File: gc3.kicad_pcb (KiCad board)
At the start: 4 copper layers, 104.6 x 77.2 mm, 204 parts, among them J1 JACK_2P, J2 DM3AT-SF-PEJM5, P1 TESTPOINT, P10 UART1, P11 CONN_01X01, P12 CONN_01X01, P13 CONN_01X01, P14 CONN_01X01, P15 TESTPOINT, P16 TESTPOINT, P17 GPIO, P18 USB_A, P19 USB_OTG, P2 TESTPOINT, P3 TESTPOINT, P4 TESTPOINT, P5 TESTPOINT, P6 TESTPOINT, P7 LCD, P8 JTAG, P9 UART0, SW1 PWR_ON, SW2 RESET, SW3 VOL+, SW4 VOL-, SW5 MENU, SW6 ENTER, SW7 HOME, U1 TPS62290, U2 axp209, U3 TPS62290, U4 a13, U5 h5tq2g63bfr, U6 TPS2552, U8 TPS2552, Y1 24MHz/20pF/10ppm

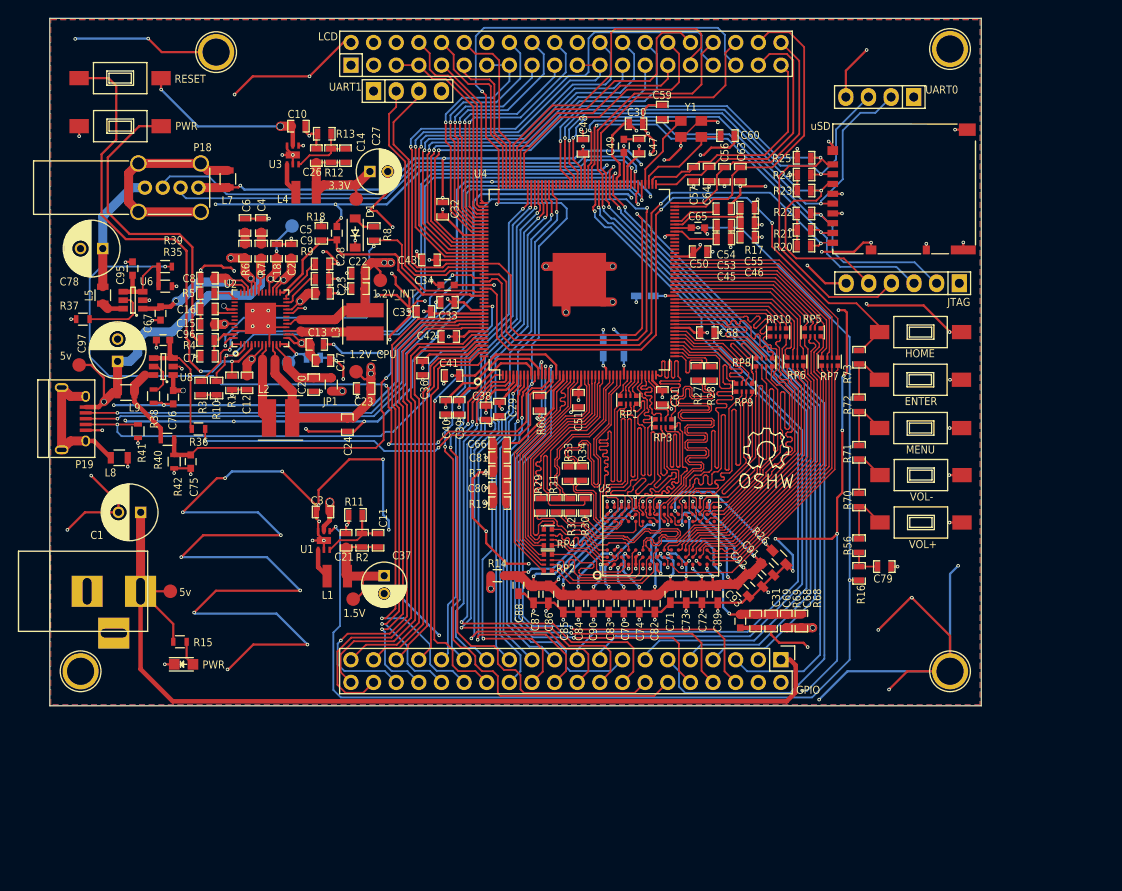
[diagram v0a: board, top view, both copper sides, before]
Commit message: clean sch and add resistor array
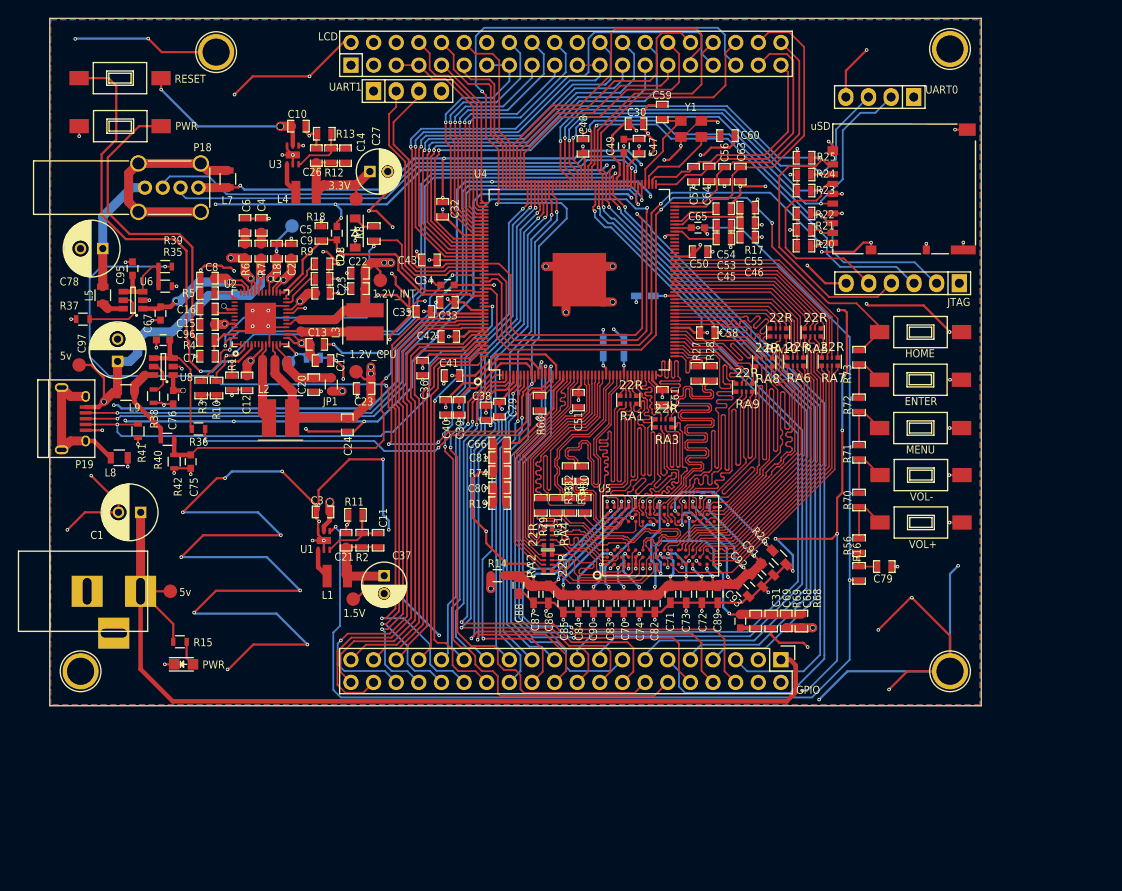
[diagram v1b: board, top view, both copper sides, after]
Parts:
- removed ?: Symbol_OSHW-Logo_SilkScreen, Symbols:Symbol_OSHW-Logo_SilkScreen
- removed RP1, RP10, RP2, RP3, RP4, RP5, RP6, RP7, RP8, RP9: R_PACK4, EXB28V:EXB28V
- added RA1: 22R, EXB28V:EXB28V, F.Cu at (170.5, 100.4)
- added RA10: 22R, EXB28V:EXB28V, F.Cu at (187.3, 92.8)
- added RA2: 22R, EXB28V:EXB28V, F.Cu at (162.9, 118.2)
- added RA3: 22R, EXB28V:EXB28V, F.Cu at (174.5, 103.0)
- added RA4: 22R, EXB28V:EXB28V, F.Cu at (162.0, 117.2)
- added RA5: 22R, EXB28V:EXB28V, F.Cu at (191.2, 92.8)
- added RA6: 22R, EXB28V:EXB28V, F.Cu at (189.3, 96.1)
- added RA7: 22R, EXB28V:EXB28V, F.Cu at (193.1, 96.1)
- added RA8: 22R, EXB28V:EXB28V, F.Cu at (185.8, 96.2)
- added RA9: 22R, EXB28V:EXB28V, F.Cu at (183.5, 99.0)
- C20: value NA or 10uF/6.3V -> 10uF/6.3V
- C27, C37: value 100uF/25V -> 100uF
- C47: value 0.1uF/6.3V -> 0.1uF
- C53: value 10uF/6.3V -> 0.1uF/6.3V
- C54: value 1uF/6.3V -> 0.1uF/6.3V
- C56, C57, C63, C64, C79: value 1nF -> 1uF
- D2: value PWR -> LED
- J1: value JACK_2P -> JACK
- L2, L3: value 2.2uH/1.5A -> 2.2uH
- P11, P12, P13, P14: value CONN_01X01 -> GND
- P16: value TESTPOINT -> TEESTPOINT
- R12: value 100K -> 100k
- R13: value 22K -> 22k
- Y1: value 24MHz/20pF/10ppm -> 24MHz/20pF/20ppm
- turned C8 to 180 degrees
- turned D1 to 270 degrees
- turned R1 to 270 degrees
- turned R16 to 270 degrees
- turned R20 to 0 degrees
- turned R21 to 0 degrees
- turned R22 to 0 degrees
- turned R23 to 0 degrees
- turned R24 to 0 degrees
- turned R25 to 0 degrees
- turned R27 to 90 degrees
- turned R28 to 90 degrees
- turned R29 to 90 degrees
- turned R30 to 90 degrees
- turned R31 to 90 degrees
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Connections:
- C14 pad 1: +3.3V -> +3V3
- C26 pad 1: +3.3V -> +3V3
- C27 pad 1: +3.3V -> +3V3
- C29 pad 1: +3.3V -> +3V3
- C30 pad 1: +3.3V -> +3V3
- C32 pad 1: +3.3V -> +3V3
- C33 pad 1: +3.3V -> +3V3
- C47 pad 1: +3.3V -> +3V3
- C8 pad 1: GND -> IPSOUT
- C8 pad 2: IPSOUT -> GND
- D1 pad 1: +3.3V -> Net-(D1-Pad1)
- D1 pad 2: Net-(D1-Pad2) -> +3V3
- J2 pad 4: +3.3V -> +3V3
- JP1 pad 1: +3.3V -> +3V3
- L4 pad 2: +3.3V -> +3V3
- P10 pad 1: +3.3V -> +3V3
- P15 pad 1: +3.3V -> +3V3
- P17 pad 3: +3.3V -> +3V3
- P7 pad 3: +3.3V -> +3V3
- P8 pad 1: +3.3V -> +3V3
- P9 pad 1: +3.3V -> +3V3
- R1 pad 1: GND -> Net-(R1-Pad1)
- R1 pad 2: Net-(R1-Pad2) -> GND
- R10 pad 2: +3.3V -> +3V3
- R12 pad 1: +3.3V -> +3V3
- R16 pad 1: +3.0VA -> Net-(C79-Pad1)
- R16 pad 2: Net-(C79-Pad1) -> +3.0VA
- R18 pad 2: +3.3V -> +3V3
- R20 pad 1: /mpu_ddr3/SD0_CARD_DETECT -> +3V3
- R20 pad 2: +3.3V -> /mpu_ddr3/SD0_CARD_DETECT
- R21 pad 1: /mpu_ddr3/SDC0_DATA1 -> +3V3
- R21 pad 2: +3.3V -> /mpu_ddr3/SDC0_DATA1
- R22 pad 1: /mpu_ddr3/SDC0_DATA0 -> +3V3
- R22 pad 2: +3.3V -> /mpu_ddr3/SDC0_DATA0
- R23 pad 1: /mpu_ddr3/SDC0_CMD -> +3V3
- R23 pad 2: +3.3V -> /mpu_ddr3/SDC0_CMD
- R24 pad 1: /mpu_ddr3/SDC0_DATA3 -> +3V3
- R24 pad 2: +3.3V -> /mpu_ddr3/SDC0_DATA3
- R25 pad 1: /mpu_ddr3/SDC0_DATA2 -> +3V3
- R25 pad 2: +3.3V -> /mpu_ddr3/SDC0_DATA2
- R27 pad 1: /mpu_ddr3/SCK -> /mpu_ddr3/CK
- R27 pad 2: /mpu_ddr3/CK -> /mpu_ddr3/SCK
- R28 pad 1: /mpu_ddr3/SCKN -> /mpu_ddr3/CKN
- R28 pad 2: /mpu_ddr3/CKN -> /mpu_ddr3/SCKN
- R29 pad 1: /mpu_ddr3/SDM1 -> /mpu_ddr3/DM1
- R29 pad 2: /mpu_ddr3/DM1 -> /mpu_ddr3/SDM1
- R3 pad 2: +3.3V -> +3V3
- R30 pad 1: /mpu_ddr3/SDM0 -> /mpu_ddr3/DM0
- R30 pad 2: /mpu_ddr3/DM0 -> /mpu_ddr3/SDM0
- R31 pad 1: /mpu_ddr3/SDQS0 -> /mpu_ddr3/DQS0
- R31 pad 2: /mpu_ddr3/DQS0 -> /mpu_ddr3/SDQS0
- R32 pad 1: /mpu_ddr3/SDQS0N -> /mpu_ddr3/DQS0N
- R32 pad 2: /mpu_ddr3/DQS0N -> /mpu_ddr3/SDQS0N
- R33 pad 1: /mpu_ddr3/SDQS1 -> /mpu_ddr3/DQS1
- R33 pad 2: /mpu_ddr3/DQS1 -> /mpu_ddr3/SDQS1
- R34 pad 1: /mpu_ddr3/SDQS1N -> /mpu_ddr3/DQS1N
- R34 pad 2: /mpu_ddr3/DQS1N -> /mpu_ddr3/SDQS1N
- R35 pad 2: +3.3V -> +3V3
- R41 pad 1: +3.3V -> +3V3
- R8 pad 1: Net-(D1-Pad2) -> /mpu_ddr3/NMI_N
- R8 pad 2: /mpu_ddr3/NMI_N -> Net-(D1-Pad1)
- SW2 pad 1: Net-(R1-Pad2) -> IPSOUT
- SW2 pad 2: IPSOUT -> Net-(R1-Pad1)
- U2 pad 4: Net-(R1-Pad2) -> Net-(R1-Pad1)
- U4 pad 100: +3.3V -> +3V3
- U4 pad 142: +3.3V -> +3V3
- U4 pad 163: +3.3V -> +3V3
- U4 pad 5: +3.3V -> +3V3
- U4 pad 97: +3.3V -> +3V3
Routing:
- net +3V3: track 0.00 -> 61.4 mm, vias 0 -> 16
- net +3.3V: track 60.3 -> 0.00 mm, vias 15 -> 0
- net Net-(R1-Pad2): track 54.0 -> 0.00 mm, vias 2 -> 0
- net Net-(R1-Pad1): track 0.00 -> 54.0 mm, vias 0 -> 2
- net Net-(D1-Pad2): track 2.48 -> 0.00 mm
- net Net-(D1-Pad1): track 0.00 -> 2.48 mm
- added copper zone on PWR.Cu, net +3V3
- removed copper zone on PWR.Cu, net +3.3V

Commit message: commit before cleanup all footprint
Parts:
- added REF**: Symbol_OSHW-Logo_SilkScreen, Symbols:Symbol_OSHW-Logo_SilkScreen, F.Cu at (186.7, 105.6)
- moved P10 2.62 mm to (144.1, 66.9)
- moved C59 1.73 mm to (175.2, 70.2)
- moved C60 0.87 mm to (182.0, 70.5), turned to 270 degrees
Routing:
- net GND: track 922.3 -> 882.3 mm, vias 190 -> 187
- net Net-(C60-Pad1): track 11.3 -> 15.1 mm
- net /mpu_ddr3/LCD_DE: track 31.8 -> 35.0 mm
- net /mpu_ddr3/LCD_CLK: track 37.9 -> 40.7 mm
- net /mpu_ddr3/LCD_HSYNC: track 25.2 -> 28.0 mm
- net /mpu_ddr3/LCD_VSYNC: track 29.2 -> 31.6 mm
- net /mpu_ddr3/UART1_RX: track 30.2 -> 28.4 mm
- net Net-(C59-Pad1): track 11.0 -> 9.53 mm
- net /mpu_ddr3/PIN6/PWM0: track 99.7 -> 98.8 mm
- net Net-(L2-Pad1): track 8.86 -> 9.66 mm
- net /mpu_ddr3/PIN8: track 102.1 -> 101.3 mm
- net /mpu_ddr3/TPY1: track 25.8 -> 25.1 mm

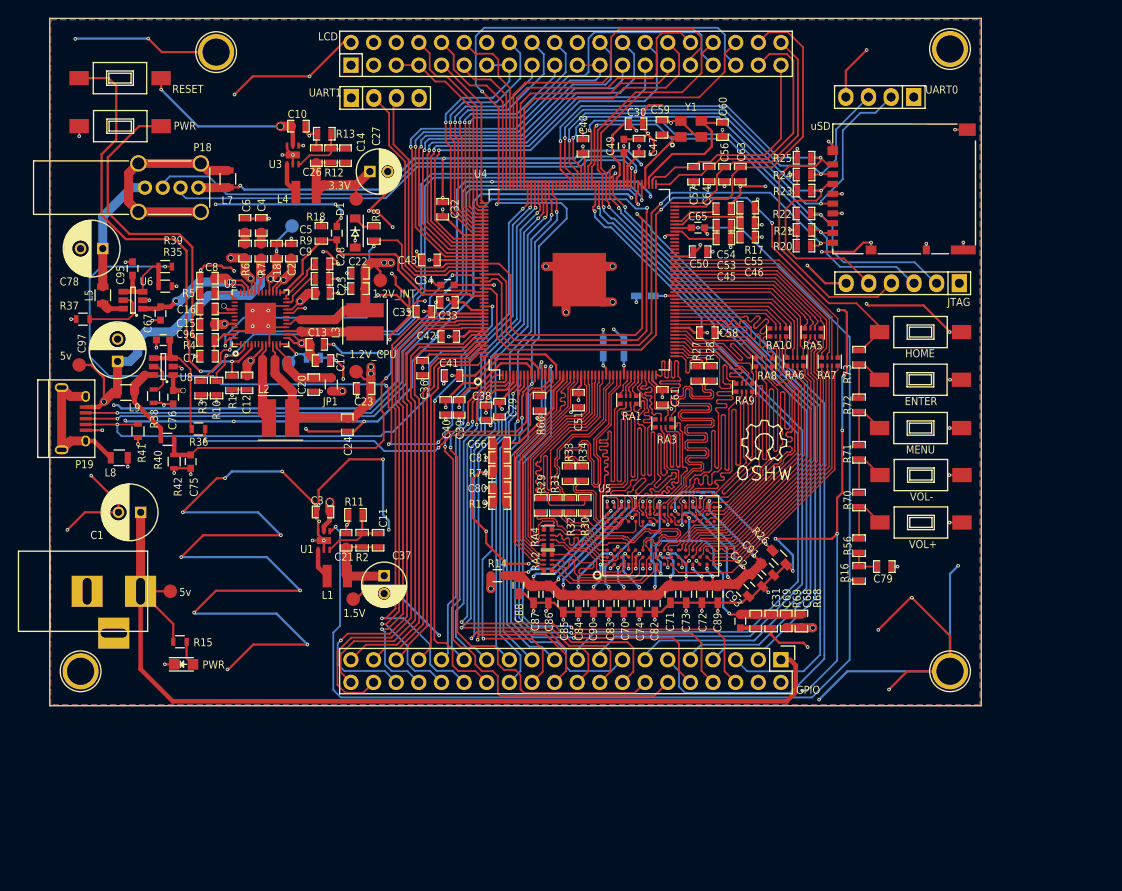
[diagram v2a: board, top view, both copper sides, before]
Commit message: clean: all footprint
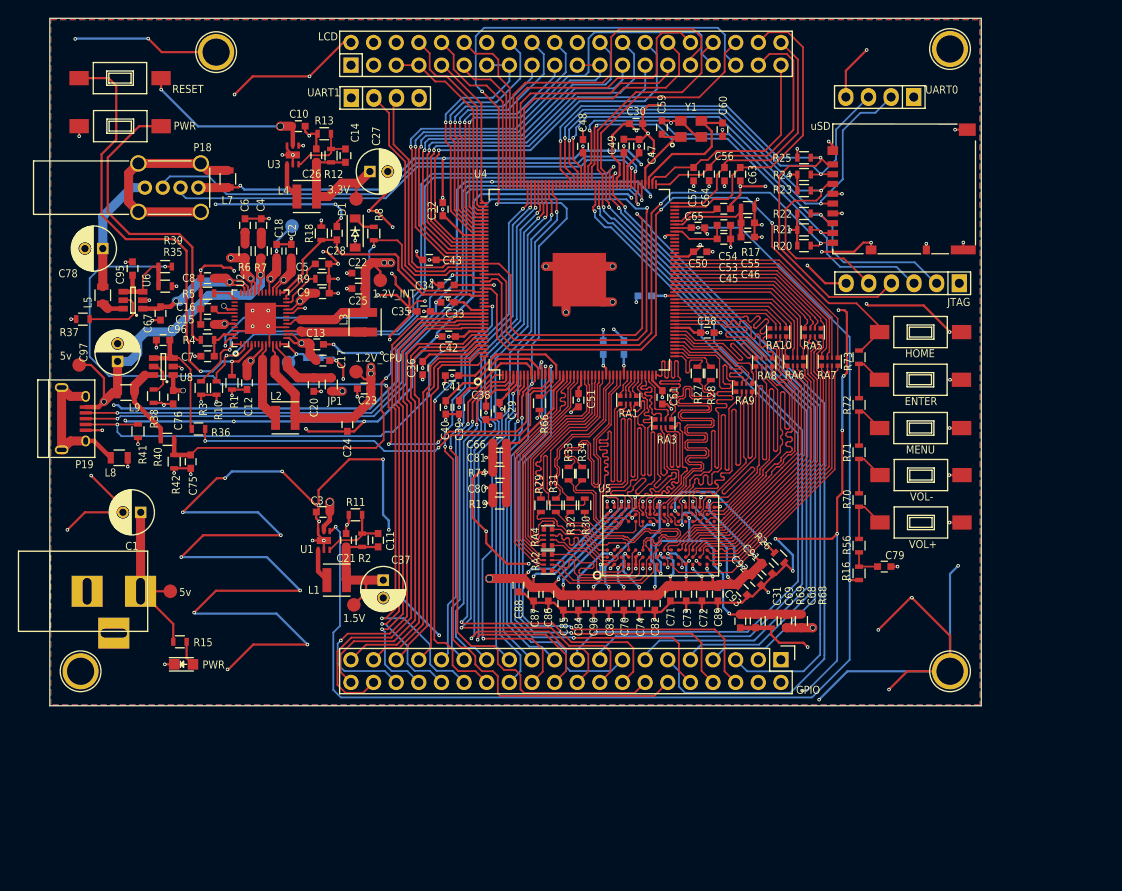
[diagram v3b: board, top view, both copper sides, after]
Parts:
- removed R14: JUMPER, Resistors_SMD:R_0603
- removed REF**: Symbol_OSHW-Logo_SilkScreen, Symbols:Symbol_OSHW-Logo_SilkScreen
- C1, C78, C97: footprint Capacitors_ThroughHole:C_Radial_D6.3_L11.2_P2.5 -> Capacitors_ThroughHole:C_Radial_D5_L11_P2
- C10, C11, C12, C13, C14, C15, C16, C17, C18, C19, C2, C20, C21, C22, C23, C24, C25, C26, C29, C3, C30, C32, C33, C35, C36, C38, C39, C4, C40, C41, C42, C43, C45, C46, C47, C48, C5, C50, C51, C53, C54, C55, C56, C57, C58, C59, C6, C60, C61, C63, C64, C66, C68, C69, C7, C79, C8, C80, C81, C9: footprint SMD_Packages:SMD-0603_c -> Capacitors_SMD:C_0603
- C44, C52, C62, C70, C71, C72, C73, C74, C82, C83, C84, C85, C86, C87, C88, C89, C90, C91, C92, C93: footprint Capacitors_SMD:C_0603_HandSoldering -> Capacitors_SMD:C_0603
- D2: value LED -> POWER
- L1, L4: footprint Inductors_NEOSID:Neosid_Inductor_SM-NE29_SMD1008 -> Inductors_NEOSID:Neosid_Inductor_SMS-ME3015
- L2, L3: footprint ELL4LG2R2NA:ELL4LG2R2NA -> Inductors_NEOSID:Neosid_Inductor_SMS-ME3015
- R1, R10, R11, R12, R13, R16, R17, R18, R19, R2, R20, R21, R22, R23, R24, R25, R27, R28, R29, R3, R30, R31, R32, R33, R34, R4, R5, R56, R6, R66, R68, R69, R7, R70, R71, R72, R73, R74, R8, R9: footprint SMD_Packages:SMD-0603_r -> Resistors_SMD:R_0603
- R26: footprint Resistors_SMD:R_0603_HandSoldering -> Resistors_SMD:R_0603
- U2: footprint axp209:TQFP-48-1EP_6x6mm_Pitch0.4mm -> AXP209:TQFP-48-1EP_6x6mm_Pitch0.4mm
- moved P6 0.65 mm to (140.6, 123.8)
- moved L2 0.53 mm to (132.9, 102.8), turned to 0 degrees
- moved C37 0.50 mm to (143.9, 121.0)
- moved L4 0.49 mm to (135.3, 78.0)
- moved L1 0.45 mm to (138.7, 121.0)
- turned L3 to 90 degrees
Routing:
- net +1.5V: track 238.2 -> 240.6 mm
- net 1.2V_INT: track 40.3 -> 41.8 mm
- net +3V3: track 61.4 -> 62.5 mm
- net Net-(L2-Pad1): track 9.66 -> 9.03 mm
- net Net-(L4-Pad1): track 3.54 -> 4.08 mm

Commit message: GC3-Update3
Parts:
- R11: value 360k -> 210k
- R2: value 540k -> 315k
- moved R16 11.6 mm to (196.0, 131.8), turned to 180 degrees
- moved C79 9.97 mm to (197.5, 129.1)
- moved R56 9.04 mm to (196.7, 126.2)
- moved SW3 8.55 mm to (201.3, 122.6)
- moved R70 6.79 mm to (196.7, 118.8)
- moved SW4 6.58 mm to (201.3, 115.1)
- moved R71 4.92 mm to (196.7, 111.6)
- moved SW5 4.92 mm to (201.3, 107.9)
- moved R22 4.73 mm to (188.1, 76.3)
- moved R25 4.65 mm to (188.1, 70.1)
- moved R24 4.56 mm to (188.1, 72.1)
- moved R23 4.37 mm to (188.1, 74.2)
- moved J2 3.64 mm to (191.1, 76.1)
- moved P12 3.63 mm to (203.9, 61.4)
- moved SW6 3.52 mm to (201.3, 100.6)
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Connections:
- U1 pad 2: GND -> IPSOUT
- U3 pad 2: GND -> IPSOUT
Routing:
- net GND: track 882.3 -> 1225.8 mm, vias 187 -> 327
- net (no net): track 0.00 -> 15.4 mm, vias 0 -> 11
- net IPSOUT: track 140.0 -> 150.9 mm, vias 11 -> 15
- net /mpu_ddr3/UBOOT: track 76.3 -> 71.0 mm
- net /mpu_ddr3/SDC0_DATA1: track 53.5 -> 48.7 mm
- net /mpu_ddr3/SDC0_SCK: track 56.4 -> 52.7 mm
- net /mpu_ddr3/SD0_CARD_DETECT: track 64.3 -> 60.7 mm
- net /mpu_ddr3/SDC0_CMD: track 62.5 -> 59.1 mm
- net /mpu_ddr3/SDC0_DATA0: track 58.1 -> 54.8 mm
- net /mpu_ddr3/UDP0: track 84.7 -> 81.8 mm
- net /mpu_ddr3/USB0_IDDET: track 126.8 -> 124.1 mm
- net /mpu_ddr3/TPY2: track 29.3 -> 26.6 mm
- net /mpu_ddr3/TPX1: track 30.6 -> 27.9 mm
- net /mpu_ddr3/TPY1: track 24.9 -> 22.5 mm
- net /mpu_ddr3/SDC0_DATA2: track 71.5 -> 69.2 mm
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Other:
- board size 104.6 x 77.2 mm -> 99.2 x 77.2 mm
